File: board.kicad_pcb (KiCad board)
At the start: 2 copper layers, 11 parts, among them J1 TEMPS, J2 OLED, J3 RELAY, J4 RELAY_EN, J5 PRGRM_INPT, U1 ESP32-WROOM-32, U2 AMS1117-3.3

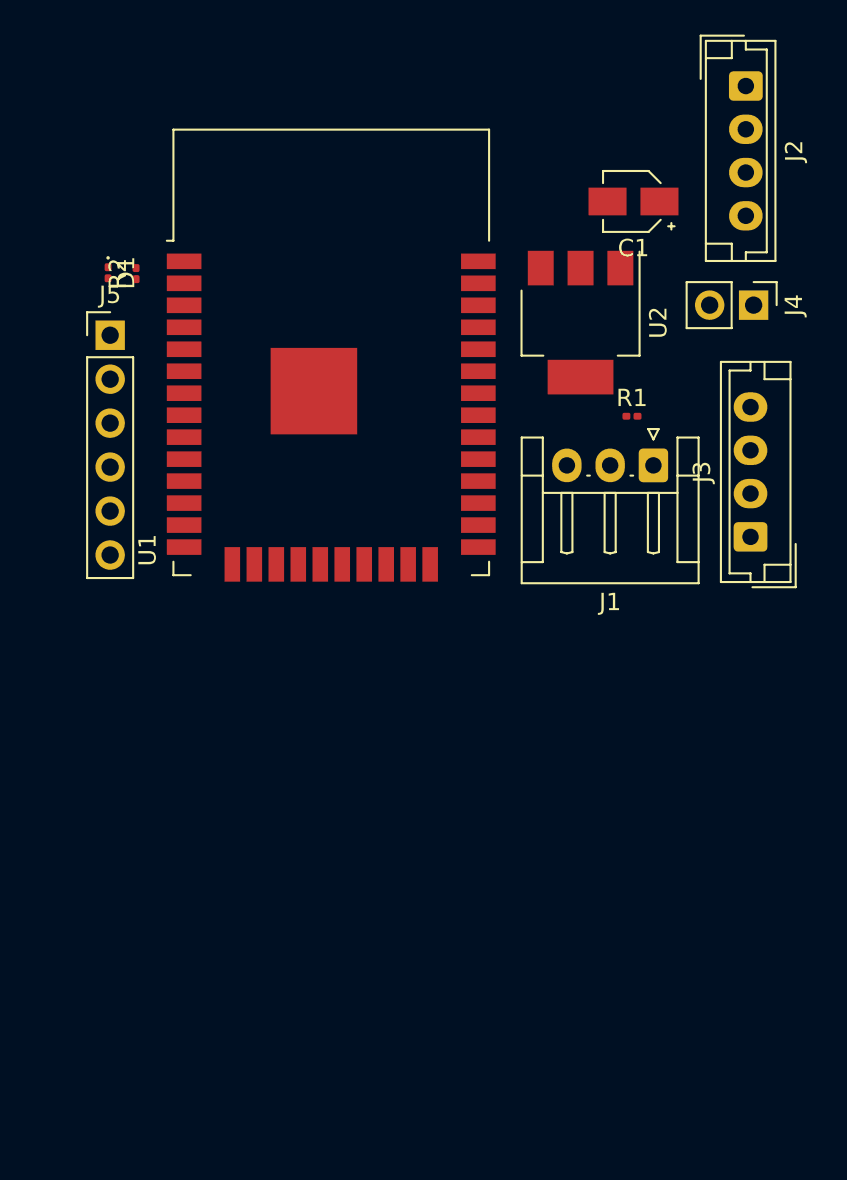
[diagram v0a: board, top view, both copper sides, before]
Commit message: added programmer, usb and general design improvements to schematic and did some measuring for final board
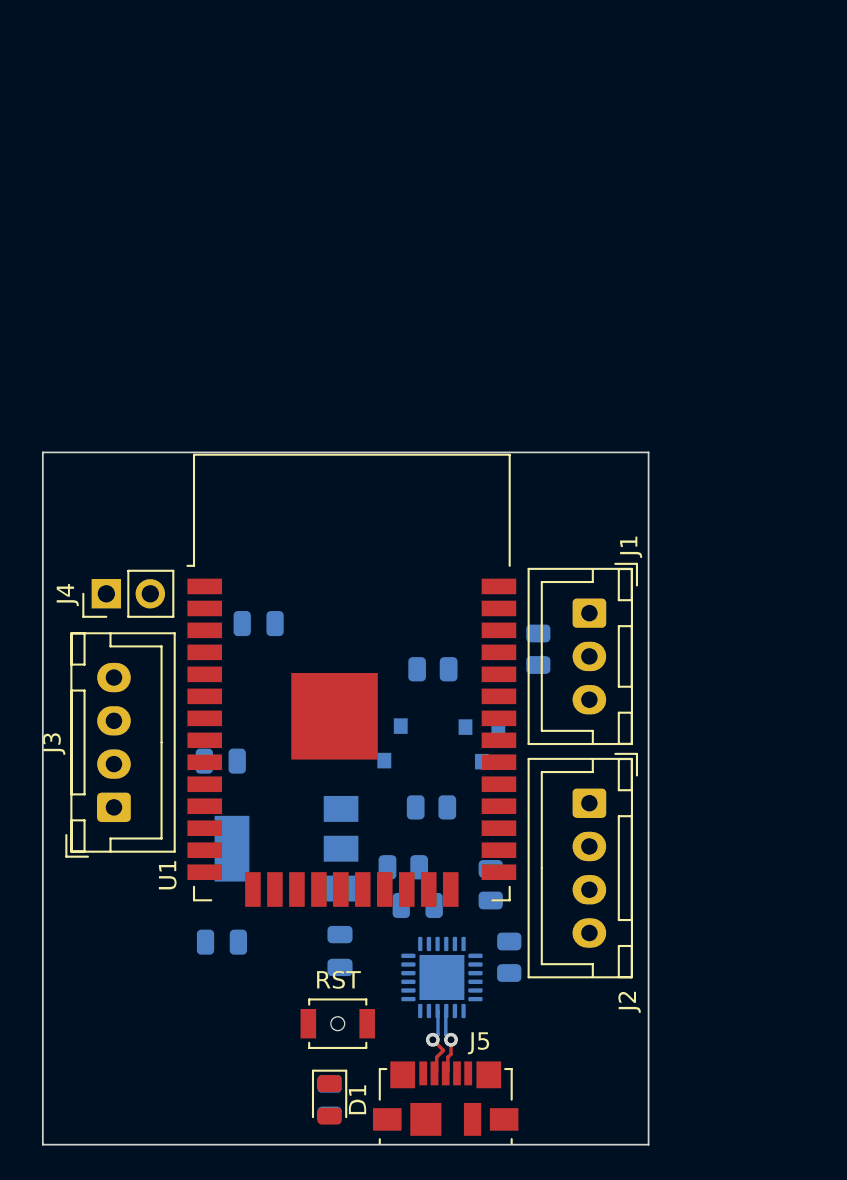
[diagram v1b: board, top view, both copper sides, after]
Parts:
- added C2: 10uF, Capacitor_SMD:C_0805_2012Metric, B.Cu at (132.5, 96.9)
- added C3: 4.7uF, Capacitor_SMD:C_0805_2012Metric, B.Cu at (141.7, 113.2)
- added C4: 100nF, Capacitor_SMD:C_0805_2012Metric, B.Cu at (130.3, 104.8)
- added C5: 10uF, Capacitor_SMD:C_0805_2012Metric, B.Cu at (130.3, 115.3)
- added Q1: BC847, Package_TO_SOT_SMD:SOT-23, B.Cu at (139.7, 103.8)
- added Q2: BC847, Package_TO_SOT_SMD:SOT-23, B.Cu at (145.4, 103.9)
- added R3: 10K, Resistor_SMD:R_0805_2012Metric, B.Cu at (140.8, 111.0)
- added R4: 470, Resistor_SMD:R_0805_2012Metric, B.Cu at (145.9, 112.0)
- added R5: 470, Resistor_SMD:R_0805_2012Metric, B.Cu at (146.9, 116.2)
- added R6: 10K, Resistor_SMD:R_0805_2012Metric, B.Cu at (142.5, 107.5)
- added R7: 10K, Resistor_SMD:R_0805_2012Metric, B.Cu at (142.5, 99.5)
- added RST: SW_RESET, Button_Switch_SMD:SW_SPST_B3U-1000P-B, F.Cu at (137.0, 120.0)
- added U3: CP2104, Package_DFN_QFN:QFN-24-1EP_4x4mm_P0.5mm_EP2.6x2.6mm, B.Cu at (143.1, 117.3)
- C1: footprint Capacitor_SMD:CP_Elec_3x5.3 -> Capacitor_SMD:C_0805_2012Metric; moved to B.Cu
- D1: footprint LED_SMD:LED_0201_0603Metric -> LED_SMD:LED_0805_2012Metric
- J1: footprint Connector_JST:JST_EH_S3B-EH_1x03_P2.50mm_Horizontal -> Connector_JST:JST_XH_B3B-XH-A_1x03_P2.50mm_Vertical
- J2, J3: footprint Connector_JST:JST_EH_B4B-EH-A_1x04_P2.50mm_Vertical -> Connector_JST:JST_XH_B4B-XH-A_1x04_P2.50mm_Vertical
- J5: value PRGRM_INPT -> USB_B_Micro; footprint Connector_PinHeader_2.54mm:PinHeader_1x06_P2.54mm_Vertical -> Connector_USB:USB_Micro-B_Molex_47346-0001
- R1, R2: footprint Resistor_SMD:R_0201_0603Metric -> Resistor_SMD:R_0805_2012Metric; moved to B.Cu
- U2: moved to B.Cu
- moved D1 49.5 mm to (136.6, 124.4)
- moved R2 49.0 mm to (136.6, 124.4), turned to 270 degrees
- moved J5 48.2 mm to (143.3, 124.3)
- moved C1 46.5 mm to (137.2, 115.8), turned to 90 degrees
- moved J2 42.4 mm to (151.6, 107.3)
- moved J4 41.0 mm to (123.7, 95.2), turned to 90 degrees
- moved J3 40.0 mm to (124.1, 107.5)
- moved U2 34.8 mm to (134.1, 109.9), turned to 180 degrees
- moved U1 18.8 mm to (137.9, 103.0)
- moved R1 14.5 mm to (148.6, 98.4), turned to 90 degrees
- moved J1 9.31 mm to (151.6, 96.3), turned to 270 degrees
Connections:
- net Net-(D1-Pad2) renamed /LED_V
- net Net-(J3-Pad4) renamed /RELAY_V
- C1 pad 2: +5V -> VBUS
- J4 pad 2: +5V -> VBUS
- J5 pad 1: Net-(J5-Pad1) -> VBUS
- J5 pad 2: Net-(J5-Pad2) -> D-
- J5 pad 3: Net-(J5-Pad3) -> D+
- J5 pad 5: Net-(J5-Pad5) -> GND
- U1 pad 25: Net-(U1-Pad25) -> GPIO0
- U1 pad 3: Net-(U1-Pad3) -> RESET
- U1 pad 34: Net-(U1-Pad34) -> /RX_ESP
- U1 pad 35: Net-(U1-Pad35) -> /TX_ESP
- U2 pad 3: +5V -> VBUS
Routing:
- net D-: track 0.00 -> 4.19 mm, vias 0 -> 1
- net D+: track 0.00 -> 3.86 mm, vias 0 -> 1
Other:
- board outline added: 35 x 40 mm

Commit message: with programmer
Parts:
- moved J4 40.3 mm to (152.8, 123.0), turned to 270 degrees
- moved J1 30.8 mm to (134.3, 121.8), turned to 90 degrees
- moved J3 27.5 mm to (151.6, 109.8), turned to 270 degrees
- moved R1 20.0 mm to (134.6, 112.7), turned to 180 degrees
- moved C5 19.4 mm to (143.8, 101.3), turned to 90 degrees
- moved R3 13.8 mm to (135.0, 98.4), turned to 180 degrees
- moved C1 12.7 mm to (143.7, 104.9), turned to 270 degrees
- moved J2 11.0 mm to (151.5, 96.3)
- moved R6 9.90 mm to (138.5, 98.4)
- moved RST 9.77 mm to (145.9, 116.0), turned to 90 degrees
- moved Q1 9.76 mm to (134.4, 95.7)
- moved D1 9.38 mm to (139.3, 115.4)
- moved R2 9.28 mm to (139.3, 115.5)
- moved R5 8.23 mm to (143.4, 108.7)
- moved U2 7.59 mm to (137.9, 103.3)
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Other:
- board size 35 x 40 mm -> 27.3 x 38.3 mm

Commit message: initial finished board pre-fab
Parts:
- removed C3: 4.7uF, Capacitor_SMD:C_0805_2012Metric
- removed Q1, Q2: BC847, Package_TO_SOT_SMD:SOT-23
- removed R6, R7: 10K, Resistor_SMD:R_0805_2012Metric
- removed RST: SW_RESET, Button_Switch_SMD:SW_SPST_B3U-1000P-B
- removed U3: CP2104, Package_DFN_QFN:QFN-24-1EP_4x4mm_P0.5mm_EP2.6x2.6mm
- added 1: MH, MountingHole:MountingHole_2.7mm_M2.5, F.Cu at (144.9, 101.4)
- added 2: MH, MountingHole:MountingHole_2.7mm_M2.5, F.Cu at (144.9, 136.1)
- added 3: MH, MountingHole:MountingHole_2.7mm_M2.5, F.Cu at (110.4, 136.1)
- added 4: MH, MountingHole:MountingHole_2.7mm_M2.5, F.Cu at (110.4, 101.4)
- added D2: PLED, LED_SMD:LED_0805_2012Metric, F.Cu at (144.9, 131.4)
- added D3: SLED2, LED_SMD:LED_0805_2012Metric, F.Cu at (118.0, 135.3)
- added G***: LOGO, Graphics:esp32_warm_water, B.Cu at (127.7, 111.5)
- added J6: CONN_PROG, Connector_PinHeader_1.27mm:PinHeader_2x05_P1.27mm_Vertical_SMD, F.Cu at (141.8, 108.5)
- added SW1: SW_RESET, Button_Switch_SMD:SW_SPST_B3U-1000P-B, F.Cu at (112.0, 112.3)
- C1, C2, C4, C5, R1, R3, U2: moved to F.Cu
- D1: value LED -> SLED1
- R2: value R -> 330; moved to F.Cu
- R4, R5: value 470 -> 330; moved to F.Cu
- moved J3 43.3 mm to (112.4, 128.2), turned to 90 degrees
- moved J4 39.5 mm to (113.9, 115.8)
- moved R5 35.4 mm to (117.2, 132.6), turned to 0 degrees
- moved C1 32.5 mm to (126.9, 132.7), turned to 0 degrees
- moved R4 31.6 mm to (120.8, 132.6), turned to 0 degrees
- moved U2 29.3 mm to (138.3, 132.7), turned to 270 degrees
- moved C4 28.5 mm to (131.2, 131.3), turned to 90 degrees
- moved D1 26.7 mm to (121.5, 135.3), turned to 90 degrees
- moved C5 26.6 mm to (135.4, 126.5)
- moved C2 23.5 mm to (110.5, 108.2), turned to 270 degrees
- moved R3 23.4 mm to (113.7, 108.2), turned to 270 degrees
- moved J2 22.4 mm to (143.0, 117.0)
- moved J5 19.2 mm to (129.9, 136.5)
- moved R2 16.5 mm to (142.9, 131.6), turned to 90 degrees
- moved U1 15.2 mm to (127.7, 114.3)
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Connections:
- net Net-(J5-Pad4) renamed /USB_4
- net Net-(J5-Pad6) renamed /USB_6
- net Net-(U1-Pad10) renamed /IO25
- net Net-(U1-Pad11) renamed /IO26
- net Net-(U1-Pad16) renamed /IO13
- net Net-(U1-Pad17) renamed /SD2
- net Net-(U1-Pad18) renamed /SD3
- net Net-(U1-Pad19) renamed /CMD
- net Net-(U1-Pad20) renamed /CLK
- net Net-(U1-Pad21) renamed /SD0
- net Net-(U1-Pad22) renamed /SD1
- net Net-(U1-Pad23) renamed /IO15
- net Net-(U1-Pad24) renamed /IO2
- net Net-(U1-Pad26) renamed /IO4
- net Net-(U1-Pad27) renamed /IO16
- net Net-(U1-Pad28) renamed /IO17
- net Net-(U1-Pad29) renamed /IO5
- net Net-(U1-Pad37) renamed /IO23
- net Net-(U1-Pad6) renamed /IO34
- net Net-(U1-Pad7) renamed /IO35
- net Net-(U1-Pad8) renamed /IO32
- net Net-(U1-Pad9) renamed /IO33
- net RESET renamed /RESET
- D1 pad 2: /LED_V -> /SLED_V1
- J5 pad 2: D- -> /USB_2
- J5 pad 3: D+ -> /USB_3
- R2 pad 2: /LED_V -> /PLED_V
- R4 pad 1: RX_CP -> SLED1
- R4 pad 2: /TX_ESP -> /SLED_V1
- R5 pad 1: /RX_ESP -> SLED2
- R5 pad 2: TX_CP -> /SLED_V2
- U1 pad 12: Net-(U1-Pad12) -> SLED2
- U1 pad 14: Net-(U1-Pad14) -> SLED1
- U1 pad 34: /RX_ESP -> RX
- U1 pad 35: /TX_ESP -> TX
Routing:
- net +3V3: track 0.00 -> 91.2 mm, vias 0 -> 3
- net VBUS: track 0.00 -> 47.7 mm, vias 0 -> 3
- net CH1: track 0.00 -> 28.7 mm, vias 0 -> 4
- net CH2: track 0.00 -> 27.5 mm, vias 0 -> 4
- net GPIO14: track 0.00 -> 18.7 mm
- net /USB_6: track 0.00 -> 17.5 mm
- net GPIO0: track 0.00 -> 17.2 mm
- net SCL: track 0.00 -> 17.0 mm, vias 0 -> 2
- net SDA: track 0.00 -> 16.2 mm, vias 0 -> 2
- net SLED2: track 0.00 -> 14.5 mm
- net /RESET: track 0.00 -> 12.7 mm, vias 0 -> 2
- net SLED1: track 0.00 -> 11.4 mm
- net /RELAY_V: track 0.00 -> 6.22 mm
- net GND: track 0.00 -> 5.64 mm, vias 0 -> 8
- net D-: track 4.19 -> 0.00 mm, vias 1 -> 0
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- added copper zone on B.Cu, net GND
- added copper zone on F.Cu, net GND
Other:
- board size 27.3 x 38.3 mm -> 40.5 x 40.7 mm
- board text added: "@wolffshots"
- board text added: "JLCJLCJLCJLC"

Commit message: straightened inset line and edited page infos
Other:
- outline, holes or cut-outs redrawn

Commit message: sourced components
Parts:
- D1, D2, D3: footprint LED_SMD:LED_0805_2012Metric -> LED_SMD:LED_0603_1608Metric
- J5: value USB_B_Micro -> PWR_IN; footprint Connector_USB:USB_Micro-B_Molex_47346-0001 -> Connector_JST:JST_XH_S2B-XH-A-1_1x02_P2.50mm_Horizontal
- J6: footprint Connector_PinHeader_1.27mm:PinHeader_2x05_P1.27mm_Vertical_SMD -> Connector_PinHeader_2.54mm:PinHeader_2x03_P2.54mm_Vertical
- SW1: footprint Button_Switch_SMD:SW_SPST_B3U-1000P-B -> Button_Switch_THT:SW_PUSH_6mm_H13mm
- moved J5 99.0 mm to (72.7, 55.6)
- moved J6 96.3 mm to (87.4, 29.0)
- moved R5 94.6 mm to (63.1, 55.0), turned to 180 degrees
- moved D3 94.3 mm to (63.0, 58.7), turned to 180 degrees
- moved SW1 94.0 mm to (58.4, 35.0), turned to 90 degrees
- moved U2 93.9 mm to (85.3, 55.0)
- moved R2 93.9 mm to (90.0, 54.0), turned to 270 degrees
- moved R4 93.9 mm to (68.0, 55.0), turned to 180 degrees
- moved D2 93.8 mm to (92.1, 53.8)
- moved 4 93.8 mm to (57.8, 23.7)
- moved 3 93.8 mm to (57.7, 58.5)
- moved 1 93.8 mm to (92.3, 23.7)
- moved G*** 93.8 mm to (75.1, 33.9)
- moved U1 93.8 mm to (75.0, 36.7)
- moved J1 93.8 mm to (73.3, 51.2)
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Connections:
- J5 pad 1: VBUS -> GND
- J5 pad 2: /USB_2 -> VBUS
- J6 pad 3: Net-(J6-Pad3) -> TX
- J6 pad 4: Net-(J6-Pad4) -> GPIO0
- J6 pad 5: Net-(J6-Pad5) -> RX
- J6 pad 6: Net-(J6-Pad6) -> +3V3
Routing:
- net /RESET: track 12.7 -> 43.7 mm
- net /USB_6: track 17.5 -> 0.00 mm
- net +3V3: track 91.2 -> 81.3 mm
- net GND: track 5.64 -> 0.00 mm, vias 8 -> 5
- net VBUS: track 47.7 -> 51.2 mm, vias 3 -> 2
- net /SLED_V2: track 1.81 -> 3.69 mm
- net /SLED_V1: track 1.82 -> 3.69 mm
- net SDA: track 16.2 -> 17.1 mm
- net /PLED_V: track 2.22 -> 2.92 mm
- net GPIO14: track 18.7 -> 19.4 mm
- net GPIO0: track 17.2 -> 16.5 mm
- net SLED1: track 11.4 -> 11.1 mm, vias 0 -> 2
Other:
- board size 40.5 x 40.7 mm -> 40.6 x 40.7 mm

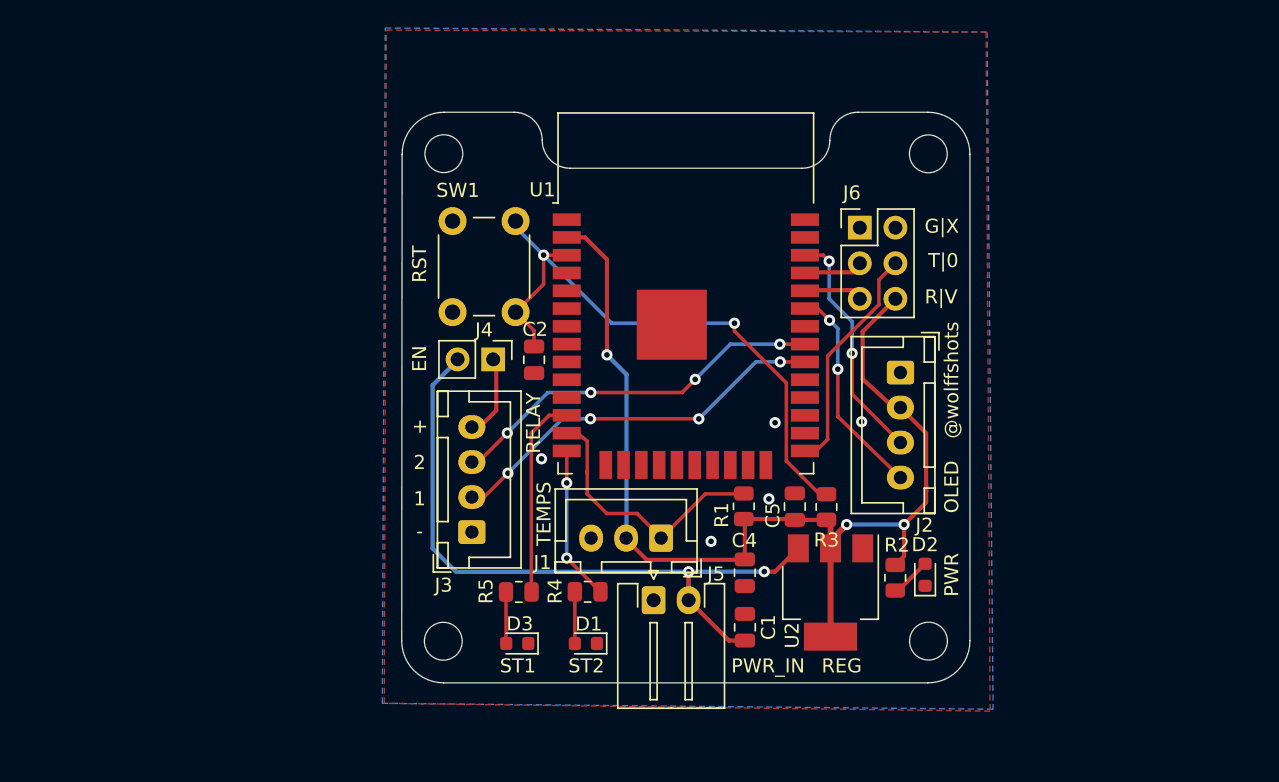
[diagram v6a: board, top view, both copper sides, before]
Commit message: feat: added usb connector and cp2104 and started redesign in kicad 6
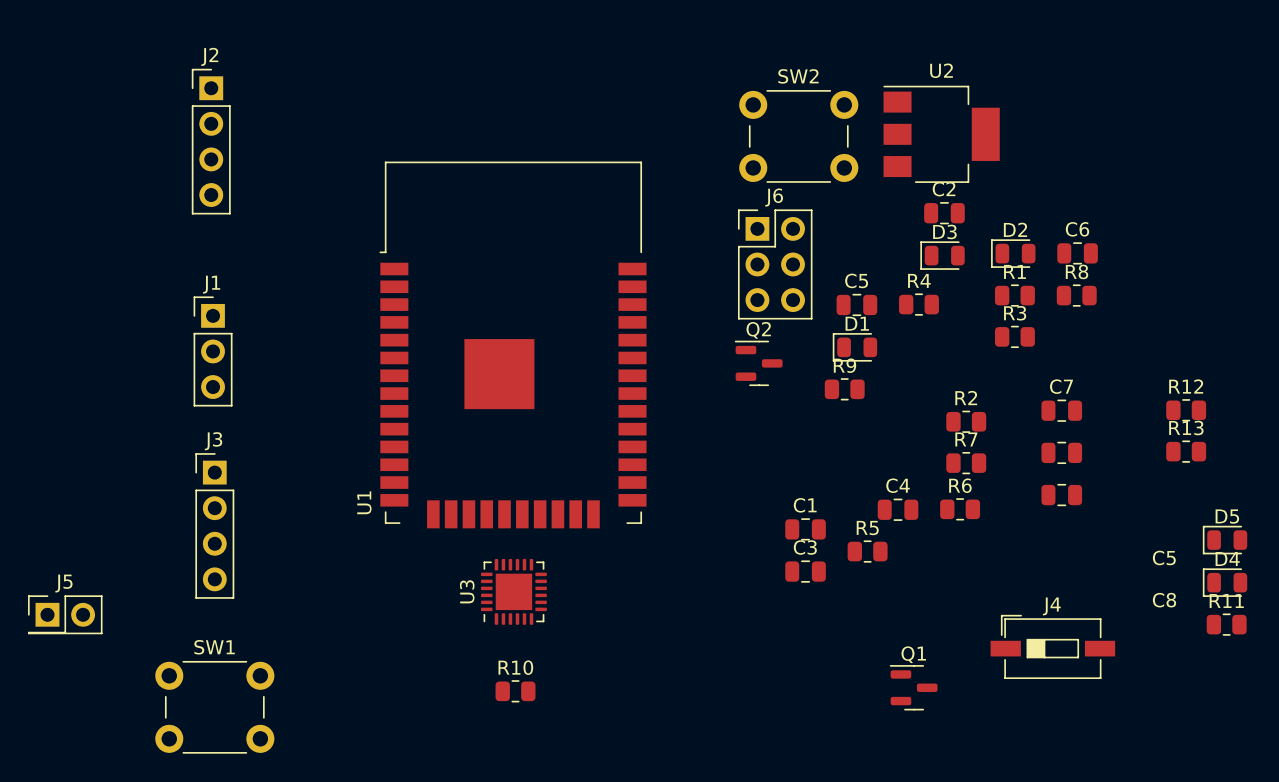
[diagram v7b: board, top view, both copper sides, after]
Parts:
- removed 1, 2, 3, 4: MH, MountingHole:MountingHole_2.7mm_M2.5
- removed the C5 at (82.8, 48.9)
- removed G***: LOGO, Graphics:esp32_warm_water
- added C3: 4.7uF, Capacitor_SMD:C_0805_2012Metric, F.Cu at (83.6, 53.6)
- added C5: 10uF, Capacitor_SMD:C_0805_2012Metric, F.Cu at (87.2, 34.5)
- added C5: 100nF, Capacitor_SMD:C_0805_2012Metric, F.Cu at (101.9, 45.1)
- added C6: 10uF, Capacitor_SMD:C_0805_2012Metric, F.Cu at (103.0, 30.8)
- added C7: 1uF, Capacitor_SMD:C_0805_2012Metric, F.Cu at (101.9, 42.1)
- added C8: 10uF, Capacitor_SMD:C_0805_2012Metric, F.Cu at (101.9, 48.1)
- added D4: TXLED, LED_SMD:LED_0805_2012Metric, F.Cu at (113.7, 54.3)
- added D5: RXLED, LED_SMD:LED_0805_2012Metric, F.Cu at (113.7, 51.3)
- added Q1: BC847, Package_TO_SOT_SMD:SOT-23, F.Cu at (91.3, 61.8)
- added Q2: BC847, Package_TO_SOT_SMD:SOT-23, F.Cu at (80.3, 38.7)
- added R10: 10k, Resistor_SMD:R_0805_2012Metric, F.Cu at (62.9, 62.1)
- added R11: 4k7, Resistor_SMD:R_0805_2012Metric, F.Cu at (113.6, 57.3)
- added R12: 4k7, Resistor_SMD:R_0805_2012Metric, F.Cu at (110.7, 42.0)
- added R13: 4k7, Resistor_SMD:R_0805_2012Metric, F.Cu at (110.7, 45.0)
- added R6: 470, Resistor_SMD:R_0805_2012Metric, F.Cu at (94.6, 49.1)
- added R7: 470, Resistor_SMD:R_0805_2012Metric, F.Cu at (95.0, 45.8)
- added R8: 10K, Resistor_SMD:R_0805_2012Metric, F.Cu at (102.9, 33.9)
- added R9: 10k, Resistor_SMD:R_0805_2012Metric, F.Cu at (86.4, 40.5)
- added SW2: SW_RST, Button_Switch_THT:SW_PUSH_6mm_H13mm, F.Cu at (79.8, 20.2)
- added U3: CP2104, Package_DFN_QFN:QFN-24-1EP_4x4mm_P0.5mm_EP2.6x2.6mm, F.Cu at (62.8, 55.0)
- D1, D2, D3: footprint LED_SMD:LED_0603_1608Metric -> LED_SMD:LED_0805_2012Metric
- J1: footprint Connector_JST:JST_XH_B3B-XH-A_1x03_P2.50mm_Vertical -> Connector_PinHeader_2.54mm:PinHeader_1x03_P2.54mm_Vertical
- J2, J3: footprint Connector_JST:JST_XH_B4B-XH-A_1x04_P2.50mm_Vertical -> Connector_PinHeader_2.54mm:PinHeader_1x04_P2.54mm_Vertical
- J4: footprint Connector_PinHeader_2.54mm:PinHeader_1x02_P2.54mm_Vertical -> Button_Switch_SMD:SW_DIP_SPSTx01_Slide_6.7x4.1mm_W6.73mm_P2.54mm_LowProfile_JPin
- J5: footprint Connector_JST:JST_XH_S2B-XH-A-1_1x02_P2.50mm_Horizontal -> Connector_PinHeader_2.54mm:PinHeader_2x01_P2.54mm_Vertical
- R2: value 330 -> 1k
- SW1: value SW_RESET -> SW_RST
- U1: value ESP32-WROOM-32 -> ESP32-WROOM-32(8MB)
- moved J2 53.2 mm to (41.1, 19.1), turned to 0 degrees
- moved J4 45.0 mm to (101.2, 59.1), turned to 0 degrees
- moved J5 43.3 mm to (29.5, 56.6)
- moved D3 41.2 mm to (93.5, 31.0), turned to 0 degrees
- moved J1 35.7 mm to (41.3, 35.3), turned to 0 degrees
- moved U2 33.7 mm to (93.3, 22.3), turned to 0 degrees
- moved SW1 32.9 mm to (38.2, 61.0), turned to 0 degrees
- moved R4 31.3 mm to (91.7, 34.5), turned to 0 degrees
- moved C2 31.1 mm to (93.5, 28.0), turned to 0 degrees
- moved D1 28.7 mm to (87.3, 37.6), turned to 0 degrees
- moved R5 25.1 mm to (88.0, 52.1), turned to 0 degrees
- moved R1 24.5 mm to (98.5, 33.9), turned to 0 degrees
- moved D2 23.8 mm to (98.6, 30.9), turned to 0 degrees
- moved J3 18.8 mm to (41.4, 46.5), turned to 0 degrees
- moved R3 18.1 mm to (98.5, 36.8), turned to 0 degrees
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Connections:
- net /RESET renamed RST
- net RX renamed RX_ESP
- net TX renamed TX_ESP
- J6 pad 2: Net-(J6-Pad2) -> unconnected-(J6-Pad2)
- U1 pad 32: Net-(U1-Pad32) -> unconnected-(U1-Pad32)
- U1 pad 4: Net-(U1-Pad4) -> unconnected-(U1-Pad4)
- U1 pad 5: Net-(U1-Pad5) -> unconnected-(U1-Pad5)
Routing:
- net +3V3: track 81.3 -> 0.00 mm, vias 3 -> 0
- net VBUS: track 51.2 -> 0.00 mm, vias 2 -> 0
- net RST: track 43.7 -> 0.00 mm, vias 2 -> 0
- net CH1: track 28.7 -> 0.00 mm, vias 4 -> 0
- net CH2: track 27.5 -> 0.00 mm, vias 4 -> 0
- net GPIO14: track 19.4 -> 0.00 mm
- net SDA: track 17.1 -> 0.00 mm, vias 2 -> 0
- net SCL: track 17.0 -> 0.00 mm, vias 2 -> 0
- net GPIO0: track 16.5 -> 0.00 mm
- net SLED2: track 14.4 -> 0.00 mm
- net SLED1: track 11.1 -> 0.00 mm, vias 2 -> 0
- net /RELAY_V: track 6.22 -> 0.00 mm
- net RX_ESP: track 3.71 -> 0.00 mm
- net TX_ESP: track 3.71 -> 0.00 mm
- net /SLED_V1: track 3.69 -> 0.00 mm
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- removed copper zone on B.Cu, net GND
- removed copper zone on F.Cu, net GND
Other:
- board outline removed
- net class Default removed
- board text removed: "@wolffshots"
- board text removed: "JLCJLCJLCJLC"
